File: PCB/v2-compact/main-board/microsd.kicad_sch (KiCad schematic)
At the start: 0 parts

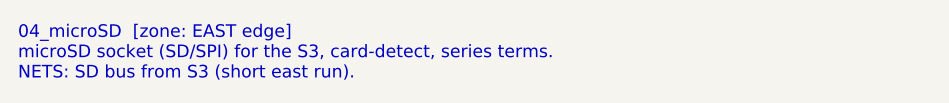
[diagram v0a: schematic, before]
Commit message: PCB: rework main board to phone-style layout; J1 -> horizontal strip
Main board (per feedback) is now a phone-style split — front is pure UI, back
carries the electronics:
- FRONT: status LEDs at the very top (above the display), TFT rotated to
  LANDSCAPE (sideways), nav buttons below it and moved down. Same feel as the
  ESP32-DIV, sideways screen.
- BACK: ESP32-S3 behind the display, microSD beside it, power + USB-C at the
  bottom-centre edge like a phone.

To keep the centre column free for the landscape display and the bottom-centre
USB-C, J1 is reoriented from a vertical 2x10 to a HORIZONTAL 10x2 strip in the
lower-centre. J1 is the shared mating datum, so the shield's J1 moves to match;
the shield's RV1106 / HTRC110 / bulk-cap zones shift to sit above/below the new
strip (SPI spine still runs north from it). Every v1 capability unchanged.

Updated both .kicad_pcb, both floorplan SVGs, both schematics' zone specs, and
PLACEMENT.md. Verified: files parse, J1 clears all zones, no same-side overlaps.

Co-Authored-By: Claude <noreply@anthropic.com>
Claude-Session: https://claude.ai/code/session_017BEAKBRVwbUCc7Sa2o3Ye7
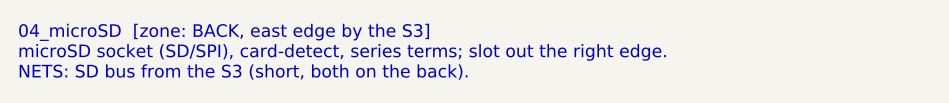
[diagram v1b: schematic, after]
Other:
- note added: "04_microSD [zone: BACK, east edge by the S3] microSD socket (SD/SPI), card-detect, series terms; slot out the right edge. NETS: SD bus from the S3 (short, both on the back)."
- note removed: "04_microSD [zone: EAST edge] microSD socket (SD/SPI) for the S3, card-detect, series terms. NETS: SD bus from S3 (short east run)."
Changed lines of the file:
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@@
   (paper "A4")
   (title_block (title "04_microSD") (company "YurilLAB"))
-  (text "04_microSD  [zone: EAST edge]
-microSD socket (SD/SPI) for the S3, card-detect, series terms.
-NETS: SD bus from S3 (short east run)." (at 15 15 0)
+  (text "04_microSD  [zone: BACK, east edge by the S3]
+microSD socket (SD/SPI), card-detect, series terms; slot out the right edge.
+NETS: SD bus from the S3 (short, both on the back)." (at 15 15 0)
     (effects (font (size 1.4 1.4)) (justify left top)))
   (sheet_instances (path "/" (page "1")))
